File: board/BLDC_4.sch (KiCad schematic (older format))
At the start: 20 parts, among them K1 SERVO, P1 HALL/Encoder, P101 CANBUS, P3 PWR_COMM, X1 MINI-USB-SHIELD-32005-201

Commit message: - changed some more Vcc labels to +3V3 - combined all input connectors into one big connector - changed can transceiver to MAX3051 - removed HV pin from power connector -> divider now on PS board - updated components - startet layout
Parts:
- removed C2: 100n, CRF1:SMD-0603_c, symbol C-RESCUE-BLDC_4
- removed K1: SERVO, CRF1:pinhead-1X03, symbol CONN_3
- removed P1: HALL/Encoder, CRF1:MICRO_JST_6, symbol CONN_6
- removed P101: CANBUS, JST conn:b4b-ph-kl, symbol CONN_4
- removed P3: PWR_COMM, CRF1:b7b-ph-kl, symbol CONN_01X07
- removed R3: 39k, CRF1:SMD-0603_r, symbol R-RESCUE-BLDC_4
- removed R4: 2k2, CRF1:SMD-0603_r, symbol R-RESCUE-BLDC_4
- removed R6: 0R, CRF1:SMD-0603_r, symbol R-RESCUE-BLDC_4
- removed X1: MINI-USB-SHIELD-32005-201, CRF1:USB-UX60R-MB-5ST, symbol MINI-USB-SCHIELD-32005-201
- added C1, C2: 100n, Capacitors_SMD:C_0805, symbol C
- added C?: 100n, symbol C
- added C?: 2u2, symbol C
- added C? (x5): 1n, symbol C
- added P1: Interface, Pin_Headers:Pin_Header_Straight_2x10, symbol CONN_01X20
- added P3: USB_B, alexmod:USBB_vert, symbol USB_B
- added U2: AP1117D33, TO_SOT_Packages_SMD:SOT-223, symbol AP1117D33
- C3: footprint CRF1:SMD-0603_c -> Capacitors_SMD:C_0805
- D1, D2, D3: footprint LEDs:LED-0603 -> LEDs:LED_0805
- P4: renamed from P?; value CONN_02X20 -> Power; footprint (none) -> Pin_Headers:Pin_Header_Straight_2x20
- R103, R104, R22, R37, R38, R5: footprint CRF1:SMD-0603_r -> Resistors_SMD:R_0805
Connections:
- net labels removed: +5V, +BATT, MISO_RX_SCL, RX_SCL_MOSI, SCK_ADC_EXT, TX_SDA, VCC
- wire segments 65 -> 86
- no-connect marks 1 -> 0
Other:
- note removed: "Mount 0R if used\nas USB host"
- moved on the sheet: C3, D1, D2, D3, P4, R103, R104, R22, R37, R38, R5

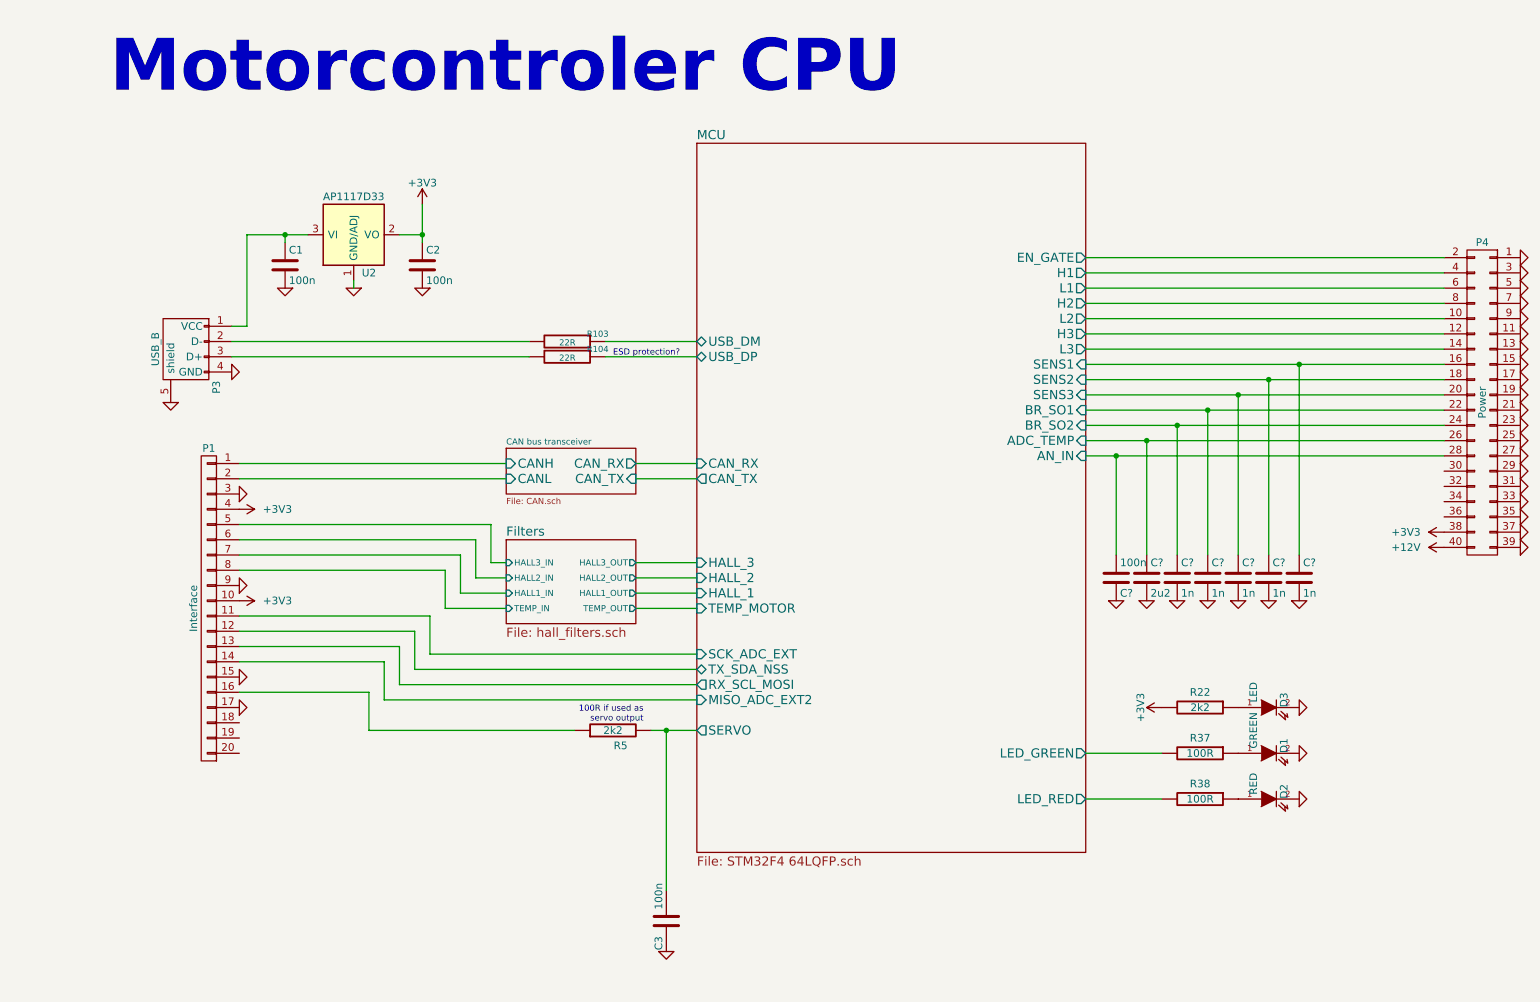
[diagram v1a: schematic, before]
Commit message: - preliminary layout for CPU board ready
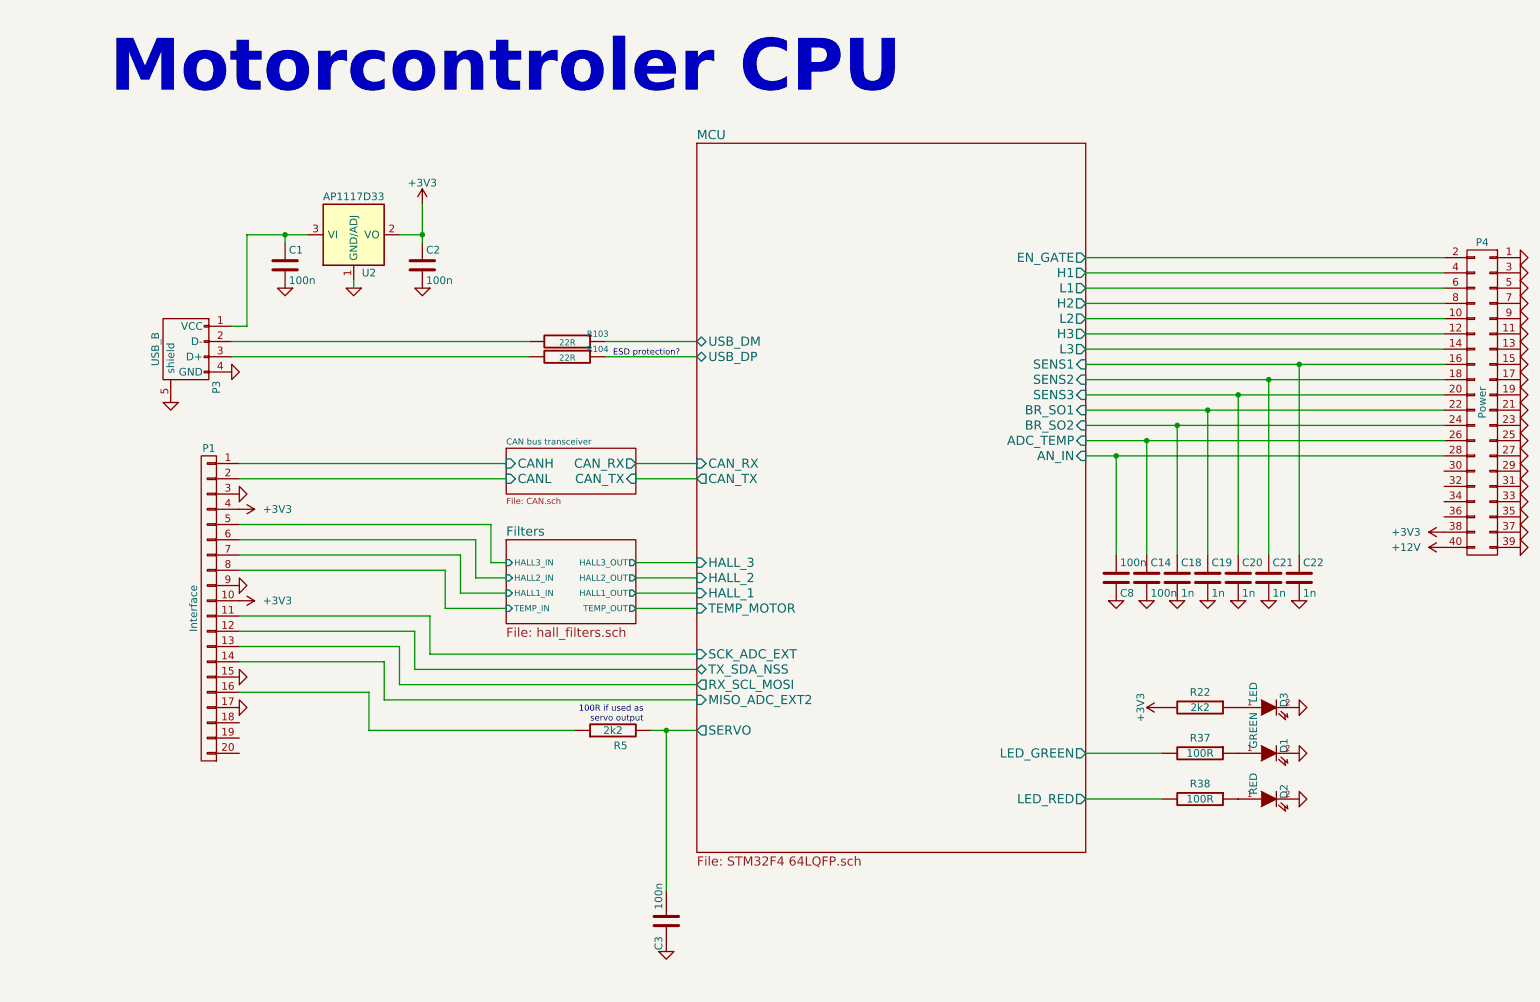
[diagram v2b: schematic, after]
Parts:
- C14: renamed from C?; value 2u2 -> 100n; footprint (none) -> Capacitors_SMD:C_0805
- C18, C19, C20, C21, C22, C8: renamed from C?; footprint (none) -> Capacitors_SMD:C_0805
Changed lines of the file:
@@
 	7550 2900 9900 2900
 Wire Wire Line
-	7550 3000 8950 3000
-Wire Wire Line
-	8950 3000 9900 3000
-Wire Wire Line
-	9900 3100 8750 3100
-Wire Wire Line
-	8750 3100 7550 3100
-Wire Wire Line
-	7550 3200 8550 3200
-Wire Wire Line
-	8550 3200 9900 3200
-Wire Wire Line
-	7550 3300 8350 3300
-Wire Wire Line
-	8350 3300 9900 3300
-Wire Wire Line
-	9900 3400 8150 3400
-Wire Wire Line
-	8150 3400 7550 3400
-Wire Wire Line
-	9900 3500 7950 3500
-Wire Wire Line
-	7950 3500 7550 3500
+	7550 3000 9900 3000
+Wire Wire Line
+	7550 3100 9900 3100
+Wire Wire Line
+	7550 3200 9900 3200
+Wire Wire Line
+	7550 3300 9900 3300
+Wire Wire Line
+	7550 3400 9900 3400
+Wire Wire Line
+	7550 3500 9900 3500
 Wire Wire Line
 	3750 3750 2000 3750
@@
 	2750 2500 2750 2450
 Wire Wire Line
-	3200 1950 3200 2150
-Wire Wire Line
-	3200 2150 3200 2200
+	3200 1950 3200 2200
 Wire Wire Line
 	3050 2150 3200 2150
 Connection ~ 3200 2150
 Wire Wire Line
-	2050 2150 2300 2150
-Wire Wire Line
-	2300 2150 2450 2150
+	2050 2150 2450 2150
 Wire Wire Line
 	2300 2150 2300 2150
@@
 	4800 6450 4800 5400
 Wire Wire Line
-	4700 5400 4800 5400
-Wire Wire Line
-	4800 5400 5000 5400
+	4700 5400 5000 5400
 Connection ~ 4800 5400
 Wire Wire Line
-	7550 3600 7750 3600
-Wire Wire Line
-	7750 3600 9900 3600
-$Comp
-L C C?
+	7550 3600 9900 3600
+$Comp
+L C C8
 U 1 1 57579789
 P 7750 4400
-F 0 "C?" H 7775 4500 50  0000 L CNN
+F 0 "C8" H 7775 4500 50  0000 L CNN
 F 1 "100n" H 7775 4300 50  0000 L CNN
-F 2 "" H 7788 4250 30  0000 C CNN
+F 2 "Capacitors_SMD:C_0805" H 7788 4250 30  0001 C CNN
 F 3 "" H 7750 4400 60  0000 C CNN
 	1    7750 4400
@@
 $EndComp
 $Comp
-L GND-RESCUE-BLDC_4 #PWR?
+L GND-RESCUE-BLDC_4 #PWR040
 U 1 1 5757A76E
 P 7750 4550
-F 0 "#PWR?" H 7750 4550 30  0001 C CNN
+F 0 "#PWR040" H 7750 4550 30  0001 C CNN
 F 1 "GND" H 7750 4480 30  0001 C CNN
 F 2 "" H 7750 4550 60  0001 C CNN
@@
 $EndComp
 $Comp
-L C C?
+L C C14
 U 1 1 5757B5D9
 P 7950 4400
-F 0 "C?" H 7975 4500 50  0000 L CNN
-F 1 "2u2" H 7975 4300 50  0000 L CNN
-F 2 "" H 7988 4250 30  0000 C CNN
+F 0 "C14" H 7975 4500 50  0000 L CNN
+F 1 "100n" H 7975 4300 50  0000 L CNN
+F 2 "Capacitors_SMD:C_0805" H 7988 4250 30  0001 C CNN
 F 3 "" H 7950 4400 60  0000 C CNN
 	1    7950 4400
@@
 $EndComp
 $Comp
-L GND-RESCUE-BLDC_4 #PWR?
+L GND-RESCUE-BLDC_4 #PWR041
 U 1 1 5757B5DF
 P 7950 4550
-F 0 "#PWR?" H 7950 4550 30  0001 C CNN
+F 0 "#PWR041" H 7950 4550 30  0001 C CNN
 F 1 "GND" H 7950 4480 30  0001 C CNN
 F 2 "" H 7950 4550 60  0001 C CNN
@@
 $EndComp
 $Comp
-L C C?
+L C C18
 U 1 1 5757B71C
 P 8150 4400
-F 0 "C?" H 8175 4500 50  0000 L CNN
+F 0 "C18" H 8175 4500 50  0000 L CNN
 F 1 "1n" H 8175 4300 50  0000 L CNN
-F 2 "" H 8188 4250 30  0000 C CNN
+F 2 "Capacitors_SMD:C_0805" H 8188 4250 30  0001 C CNN
 F 3 "" H 8150 4400 60  0000 C CNN
 	1    8150 4400
@@
 $EndComp
 $Comp
-L GND-RESCUE-BLDC_4 #PWR?
+L GND-RESCUE-BLDC_4 #PWR042
 U 1 1 5757B722
 P 8150 4550
-F 0 "#PWR?" H 8150 4550 30  0001 C CNN
+F 0 "#PWR042" H 8150 4550 30  0001 C CNN
 F 1 "GND" H 8150 4480 30  0001 C CNN
 F 2 "" H 8150 4550 60  0001 C CNN
@@
 $EndComp
 $Comp
-L C C?
+L C C19
 U 1 1 5757C86F
 P 8350 4400
-F 0 "C?" H 8375 4500 50  0000 L CNN
+F 0 "C19" H 8375 4500 50  0000 L CNN
 F 1 "1n" H 8375 4300 50  0000 L CNN
-F 2 "" H 8388 4250 30  0000 C CNN
+F 2 "Capacitors_SMD:C_0805" H 8388 4250 30  0001 C CNN
 F 3 "" H 8350 4400 60  0000 C CNN
 	1    8350 4400
@@
 $EndComp
 $Comp
-L GND-RESCUE-BLDC_4 #PWR?
+L GND-RESCUE-BLDC_4 #PWR043
 U 1 1 5757C875
 P 8350 4550
-F 0 "#PWR?" H 8350 4550 30  0001 C CNN
+F 0 "#PWR043" H 8350 4550 30  0001 C CNN
 F 1 "GND" H 8350 4480 30  0001 C CNN
 F 2 "" H 8350 4550 60  0001 C CNN
@@
 Connection ~ 8350 3300
 $Comp
-L C C?
+L C C20
 U 1 1 5757FA6D
 P 8550 4400
-F 0 "C?" H 8575 4500 50  0000 L CNN
+F 0 "C20" H 8575 4500 50  0000 L CNN
 F 1 "1n" H 8575 4300 50  0000 L CNN
-F 2 "" H 8588 4250 30  0000 C CNN
+F 2 "Capacitors_SMD:C_0805" H 8588 4250 30  0001 C CNN
 F 3 "" H 8550 4400 60  0000 C CNN
 	1    8550 4400
@@
 $EndComp
 $Comp
-L GND-RESCUE-BLDC_4 #PWR?
+L GND-RESCUE-BLDC_4 #PWR044
 U 1 1 5757FA73
 P 8550 4550
-F 0 "#PWR?" H 8550 4550 30  0001 C CNN
+F 0 "#PWR044" H 8550 4550 30  0001 C CNN
 F 1 "GND" H 8550 4480 30  0001 C CNN
 F 2 "" H 8550 4550 60  0001 C CNN
@@
 $EndComp
 $Comp
-L C C?
+L C C21
 U 1 1 5757FA79
 P 8750 4400
-F 0 "C?" H 8775 4500 50  0000 L CNN
+F 0 "C21" H 8775 4500 50  0000 L CNN
 F 1 "1n" H 8775 4300 50  0000 L CNN
-F 2 "" H 8788 4250 30  0000 C CNN
+F 2 "Capacitors_SMD:C_0805" H 8788 4250 30  0001 C CNN
 F 3 "" H 8750 4400 60  0000 C CNN
 	1    8750 4400
@@
 $EndComp
 $Comp
-L GND-RESCUE-BLDC_4 #PWR?
+L GND-RESCUE-BLDC_4 #PWR045
 U 1 1 5757FA7F
 P 8750 4550
-F 0 "#PWR?" H 8750 4550 30  0001 C CNN
+F 0 "#PWR045" H 8750 4550 30  0001 C CNN
 F 1 "GND" H 8750 4480 30  0001 C CNN
 F 2 "" H 8750 4550 60  0001 C CNN
@@
 $EndComp
 $Comp
-L C C?
+L C C22
 U 1 1 5757FA85
 P 8950 4400
-F 0 "C?" H 8975 4500 50  0000 L CNN
+F 0 "C22" H 8975 4500 50  0000 L CNN
 F 1 "1n" H 8975 4300 50  0000 L CNN
-F 2 "" H 8988 4250 30  0000 C CNN
+F 2 "Capacitors_SMD:C_0805" H 8988 4250 30  0001 C CNN
 F 3 "" H 8950 4400 60  0000 C CNN
 	1    8950 4400
@@
 $EndComp
 $Comp
-L GND-RESCUE-BLDC_4 #PWR?
+L GND-RESCUE-BLDC_4 #PWR046
 U 1 1 5757FA8B
 P 8950 4550
-F 0 "#PWR?" H 8950 4550 30  0001 C CNN
+F 0 "#PWR046" H 8950 4550 30  0001 C CNN
 F 1 "GND" H 8950 4480 30  0001 C CNN
 F 2 "" H 8950 4550 60  0001 C CNN
